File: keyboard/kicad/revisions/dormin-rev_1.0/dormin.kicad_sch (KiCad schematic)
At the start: 109 parts, among them J2 Conn_01x04_Pin, J3 Pogo Connector, Q1 HX2302A, SW1 SW_Push, SW10 SW_Push, SW11 SW_Push, SW12 SW_Push, SW13 SW_Push, SW14 SW_Push, SW15 SW_Push, SW16 SW_Push, SW17 SW_Push, SW18 SW_Push, SW19 SW_Push, SW2 SW_Push, SW20 SW_Push, SW3 SW_Push, SW4 SW_Push, SW5 SW_Push, SW6 SW_Push, SW7 SW_Push, SW8 SW_Push, SW9 SW_Push, U3 XIAO-nRF52840-Plus-SMD, U4 TPD2E2U06DCK

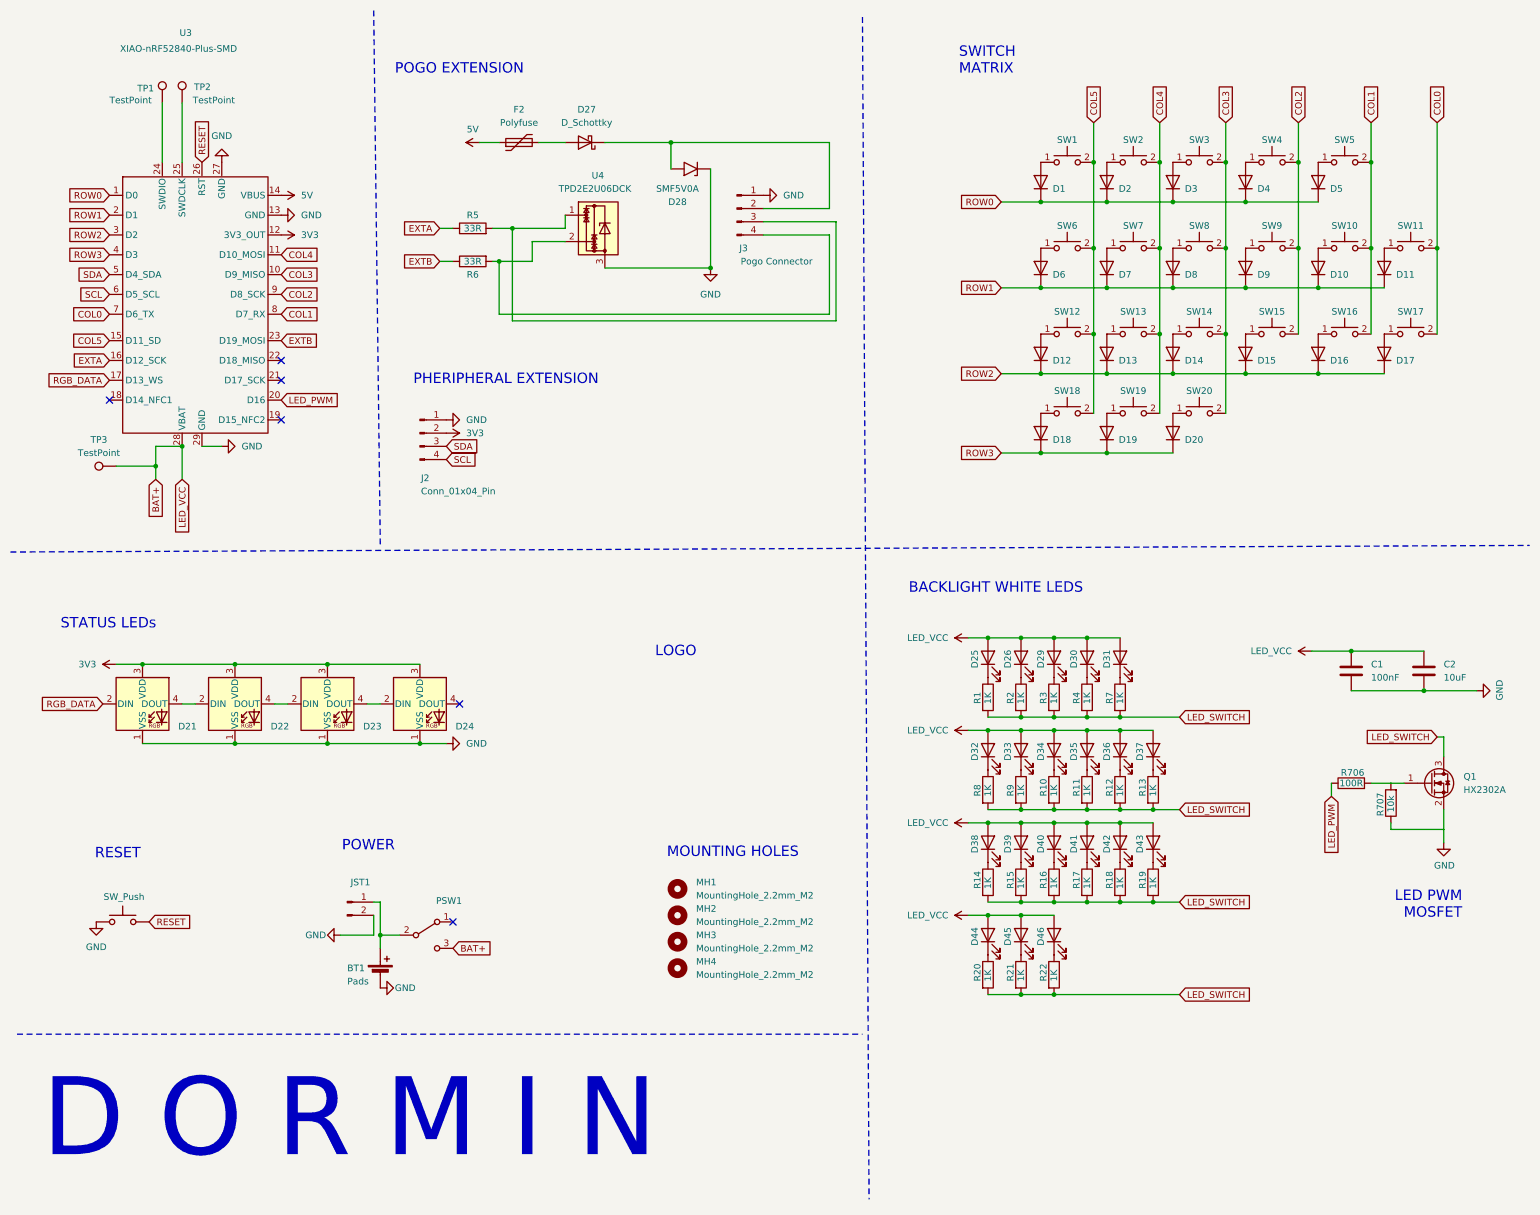
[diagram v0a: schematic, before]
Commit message: feat: added 3dmodels and improve components placement
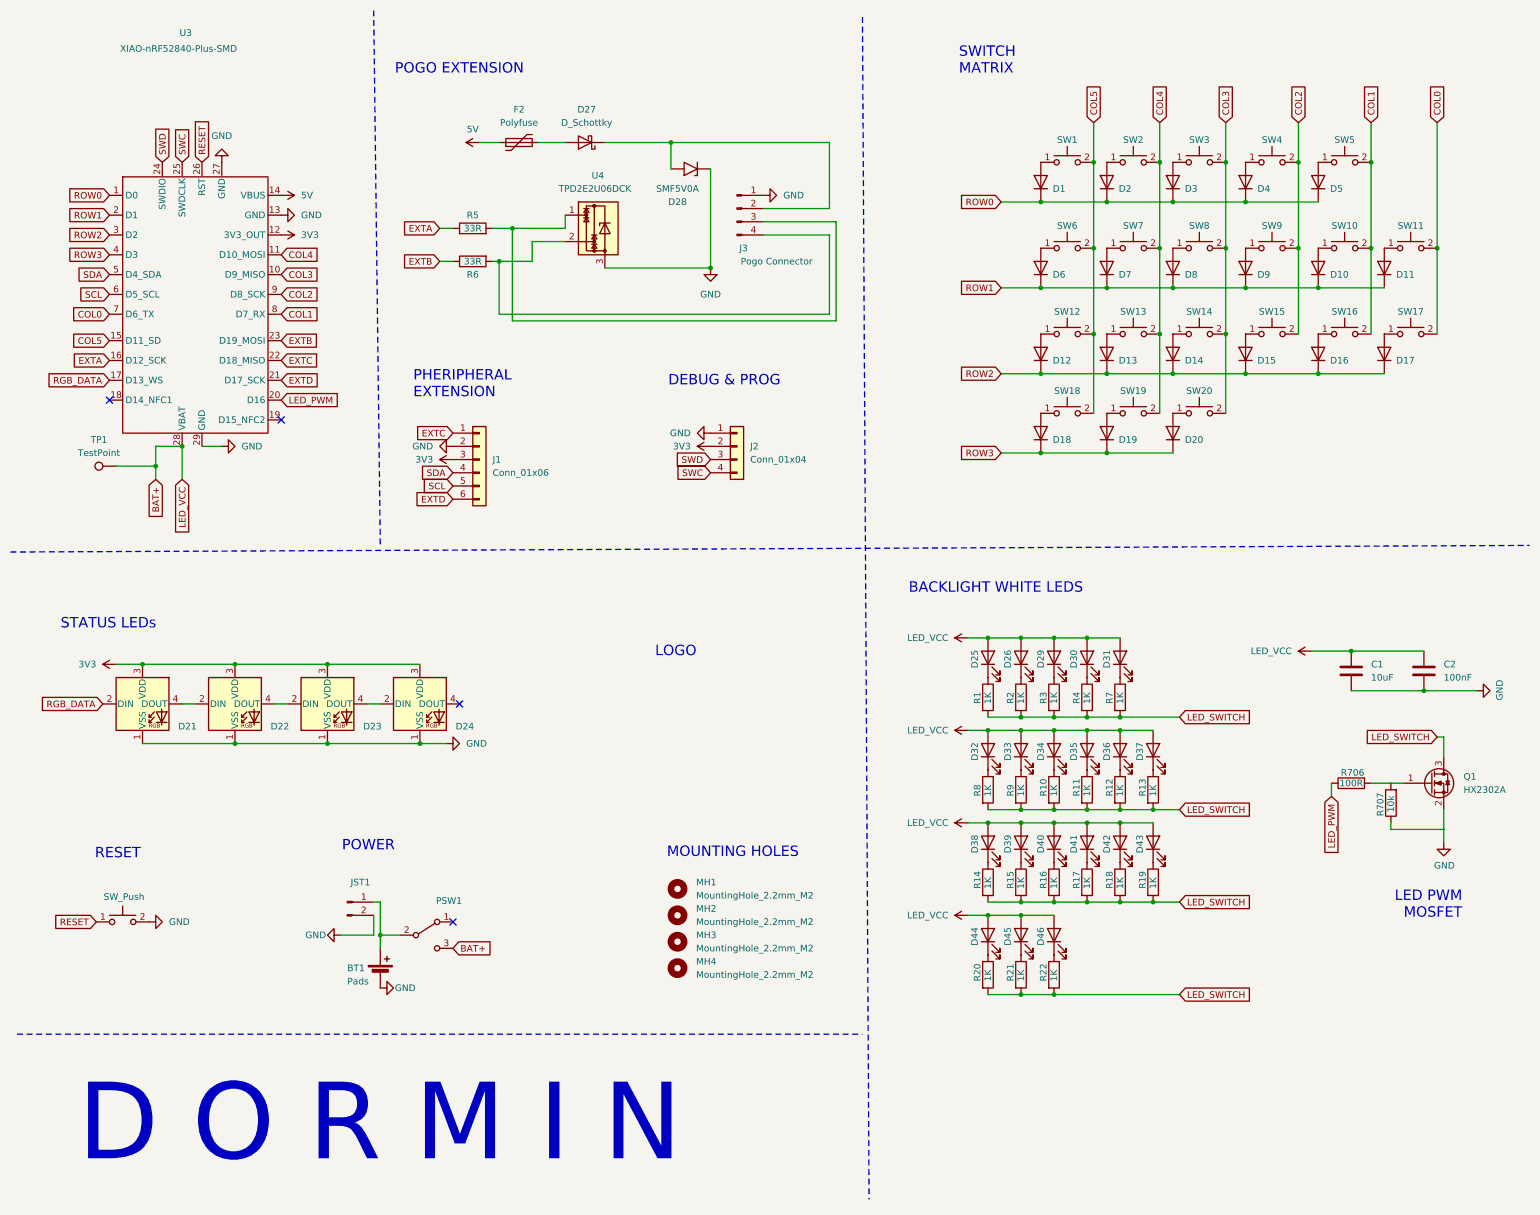
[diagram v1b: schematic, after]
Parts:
- removed J2: Conn_01x04_Pin, symbol Connector:Conn_01x04_Pin
- removed TP1, TP2: TestPoint, symbol Connector:TestPoint
- added J1: Conn_01x06, Connector_PinSocket_1.00mm:PinSocket_1x06_P1.00mm_Vertical, symbol Connector_Generic:Conn_01x06
- added J2: Conn_01x04, Connector_PinSocket_1.00mm:PinSocket_1x04_P1.00mm_Vertical, symbol Connector_Generic:Conn_01x04
- C1: value 100nF -> 10uF
- C2: value 10uF -> 100nF
- J3: footprint Connector_PinSocket_2.54mm:PinSocket_1x04_P2.54mm_Vertical_SMD_Pin1Left -> willkeebs_components:MAGNET_CONN_5x2_54mm_THT
- renumbered TP3 to TP1
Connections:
- net 3V3: now also J1.3 (Pin_3), J2.2 (Pin_2)
- net GND: now also RSW1.2, J1.2 (Pin_2), J2.1 (Pin_1); no longer RSW1.1
- net RESET: now also RSW1.1; no longer RSW1.2
- net SCL: now also J1.5 (Pin_5)
- net SDA: now also J1.4 (Pin_4)
- net SWC: now reaches U3.25 (SWDCLK)
- net SWC: now also J2.4 (Pin_4)
- net SWD: now reaches U3.24 (SWDIO)
- net SWD: now also J2.3 (Pin_3)
- net EXTD: now reaches U3.21 (D17_SCK)
- net EXTD: now also J1.6 (Pin_6)
- net EXTC: now reaches U3.22 (D18_MISO)
- net EXTC: now also J1.1 (Pin_1)
- no-connect marks 6 -> 4
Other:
- note added: "DEBUG & PROG"

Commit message: feat: updated schematics
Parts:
- removed J3: Pogo Connector, willkeebs_components:MAGNET_CONN_5x2_54mm_THT, symbol Connector:Conn_01x04_Pin
- added J4: Conn_01x04, Connector_PinSocket_2.54mm:PinSocket_1x04_P2.54mm_Vertical, symbol Connector_Generic:Conn_01x04
- J1: footprint Connector_PinSocket_1.00mm:PinSocket_1x06_P1.00mm_Vertical -> Connector_PinSocket_2.54mm:PinSocket_1x06_P2.54mm_Vertical
- J2: footprint Connector_PinSocket_1.00mm:PinSocket_1x04_P1.00mm_Vertical -> Connector_PinSocket_2.54mm:PinSocket_1x04_P2.54mm_Vertical
- RSW1: value SW_Push -> RSW1
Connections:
- net EXTC is gone; now on net EXTA: J1.1 (Pin_1), U3.22 (D18_MISO)
- net EXTD is gone; now on net EXTB: J1.6 (Pin_6), U3.21 (D17_SCK)
- net COL0: now also U3.15 (D11_SD); no longer U3.7 (D6_TX)
- net COL1: now also U3.16 (D12_SCK); no longer U3.8 (D7_RX)
- net COL5: now also U3.23 (D19_MOSI); no longer U3.15 (D11_SD)
- net EXTA: no longer R5.1, U3.16 (D12_SCK)
- net EXTB: no longer R6.1, U3.23 (D19_MOSI)
- net GND: now also J4.1 (Pin_1)
- net at R5.2, U4.1: now also J4.3 (Pin_3)
- net at D27.1 (K), D28.2 (A2): now also J4.2 (Pin_2)
- net at R6.2, U4.2: now also J4.4 (Pin_4)
- net VBAT_RAW: now reaches BT1.1 (+), JST1.1 (Pin_1), PSW1.2 (B)
- net LED_VCC renamed VBAT
- new net RX: R6.1, U3.8 (D7_RX)
- new net TX: R5.1, U3.7 (D6_TX)
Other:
- moved on the sheet: BT1, D27, D28, F2, JST1, PSW1, R5, R6, TP1, U4

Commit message: feat: organize pcb components placements
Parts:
- removed J4: Conn_01x04, Connector_PinSocket_2.54mm:PinSocket_1x04_P2.54mm_Vertical, symbol Connector_Generic:Conn_01x04
- added J3: Conn_01x05, willkeebs_misc:SMD_Conn_1x04_P2.54mm_Vertical, symbol Connector_Generic:Conn_01x05
- added R23: 100R, Resistor_SMD:R_0402_1005Metric, symbol Device:R
- J1: footprint Connector_PinSocket_2.54mm:PinSocket_1x06_P2.54mm_Vertical -> willkeebs_misc:SMD_Conn_1x06_P2.54mm_Vertical
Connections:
- net EXTA: now also U3.21 (D17_SCK); no longer U3.22 (D18_MISO)
- net EXTB: now also U3.22 (D18_MISO); no longer U3.21 (D17_SCK)
- net GND: now also J3.1 (Pin_1)
- net SCL: now also J1.4 (Pin_4); no longer J1.5 (Pin_5)
- net SDA: now also J1.5 (Pin_5); no longer J1.4 (Pin_4)
- net SWC: now also J2.3 (Pin_3); no longer J2.4 (Pin_4)
- net SWD: now also J2.4 (Pin_4); no longer J2.3 (Pin_3)
- net at R5.2, U4.1: now also J3.4 (Pin_4)
- net at D27.1 (K), D28.2 (A2): now also J3.2 (Pin_2)
- net at R6.2, U4.2: now also J3.3 (Pin_3)
- net DETECT: now reaches U3.18 (D14_NFC1)
- net DETECT: now also R23.1
- new net: J3.5 (Pin_5), R23.2
- no-connect marks 4 -> 3
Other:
- note added: "DEBUG"
- note added: "EXTENTIONS"
- note added: "PHERIPHERAL"
- note added: "POGO Connector"
- note removed: "DEBUG & PROG"
- note removed: "PHERIPHERAL EXTENSION"
- note removed: "POGO EXTENSION"
- moved on the sheet: D27, D28, F2, J1, R5, R6, U4

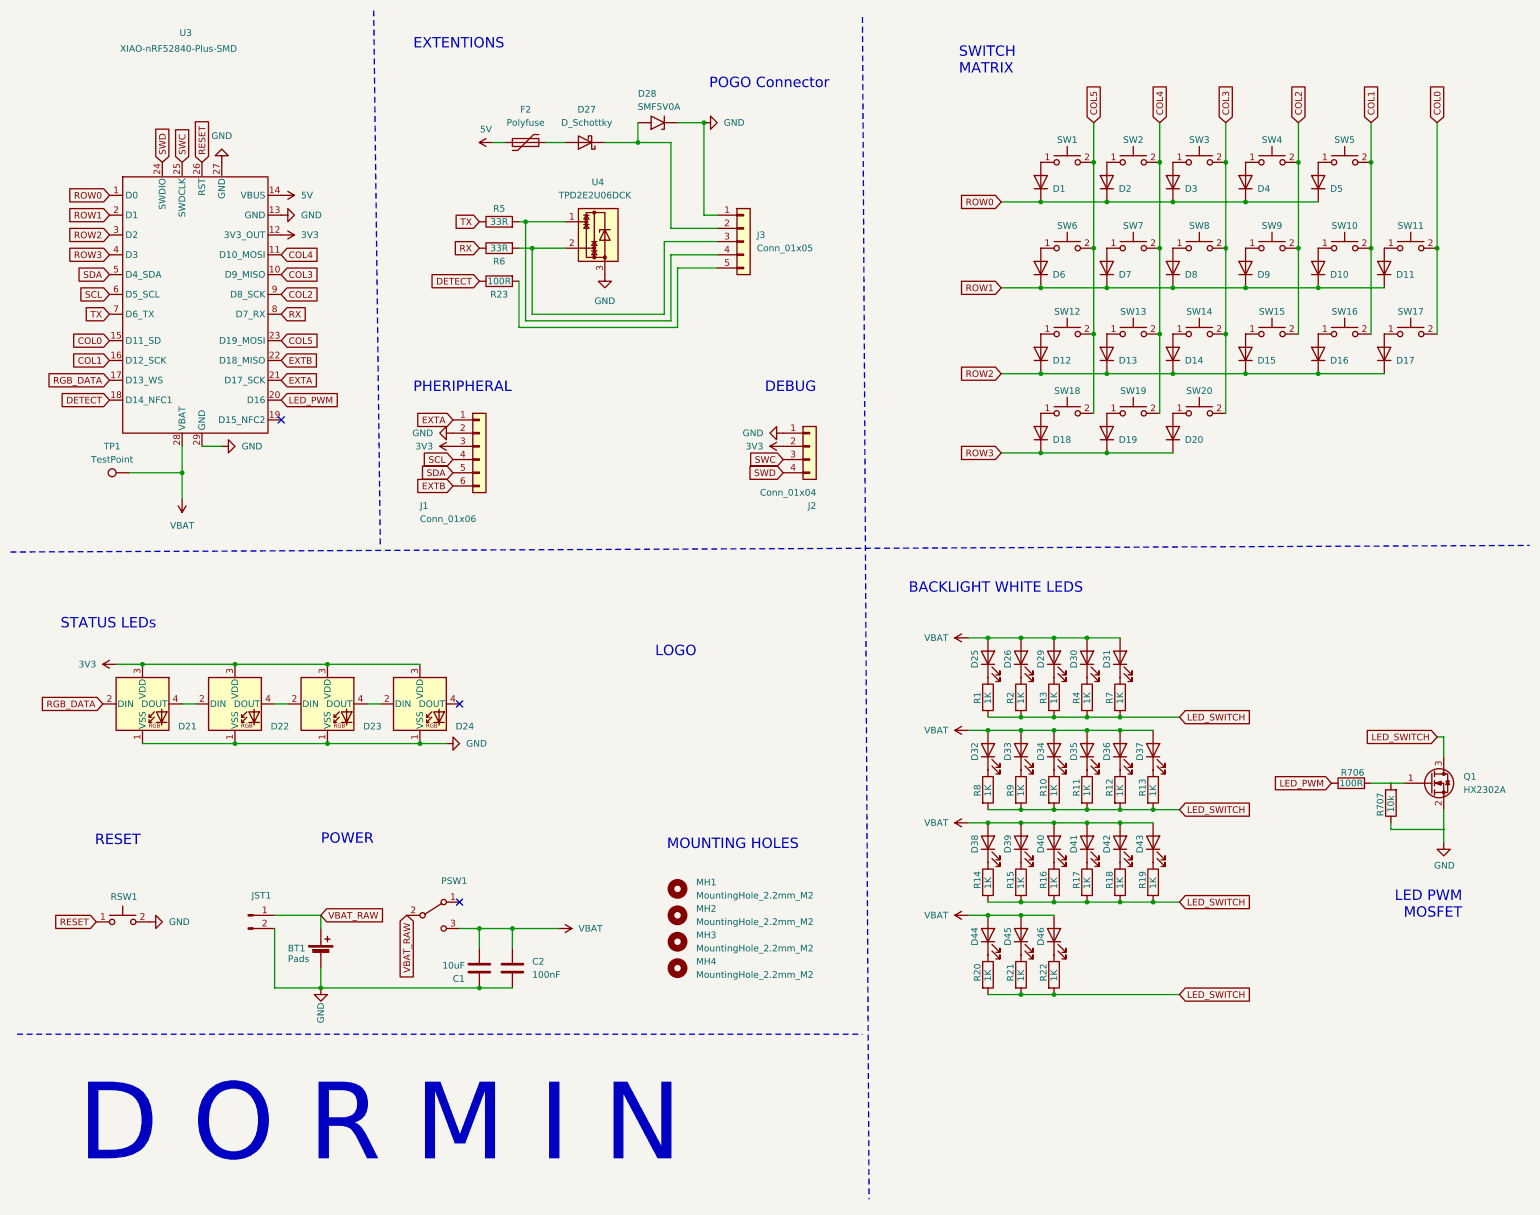
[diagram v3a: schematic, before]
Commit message: feat: implemented better status-led-system
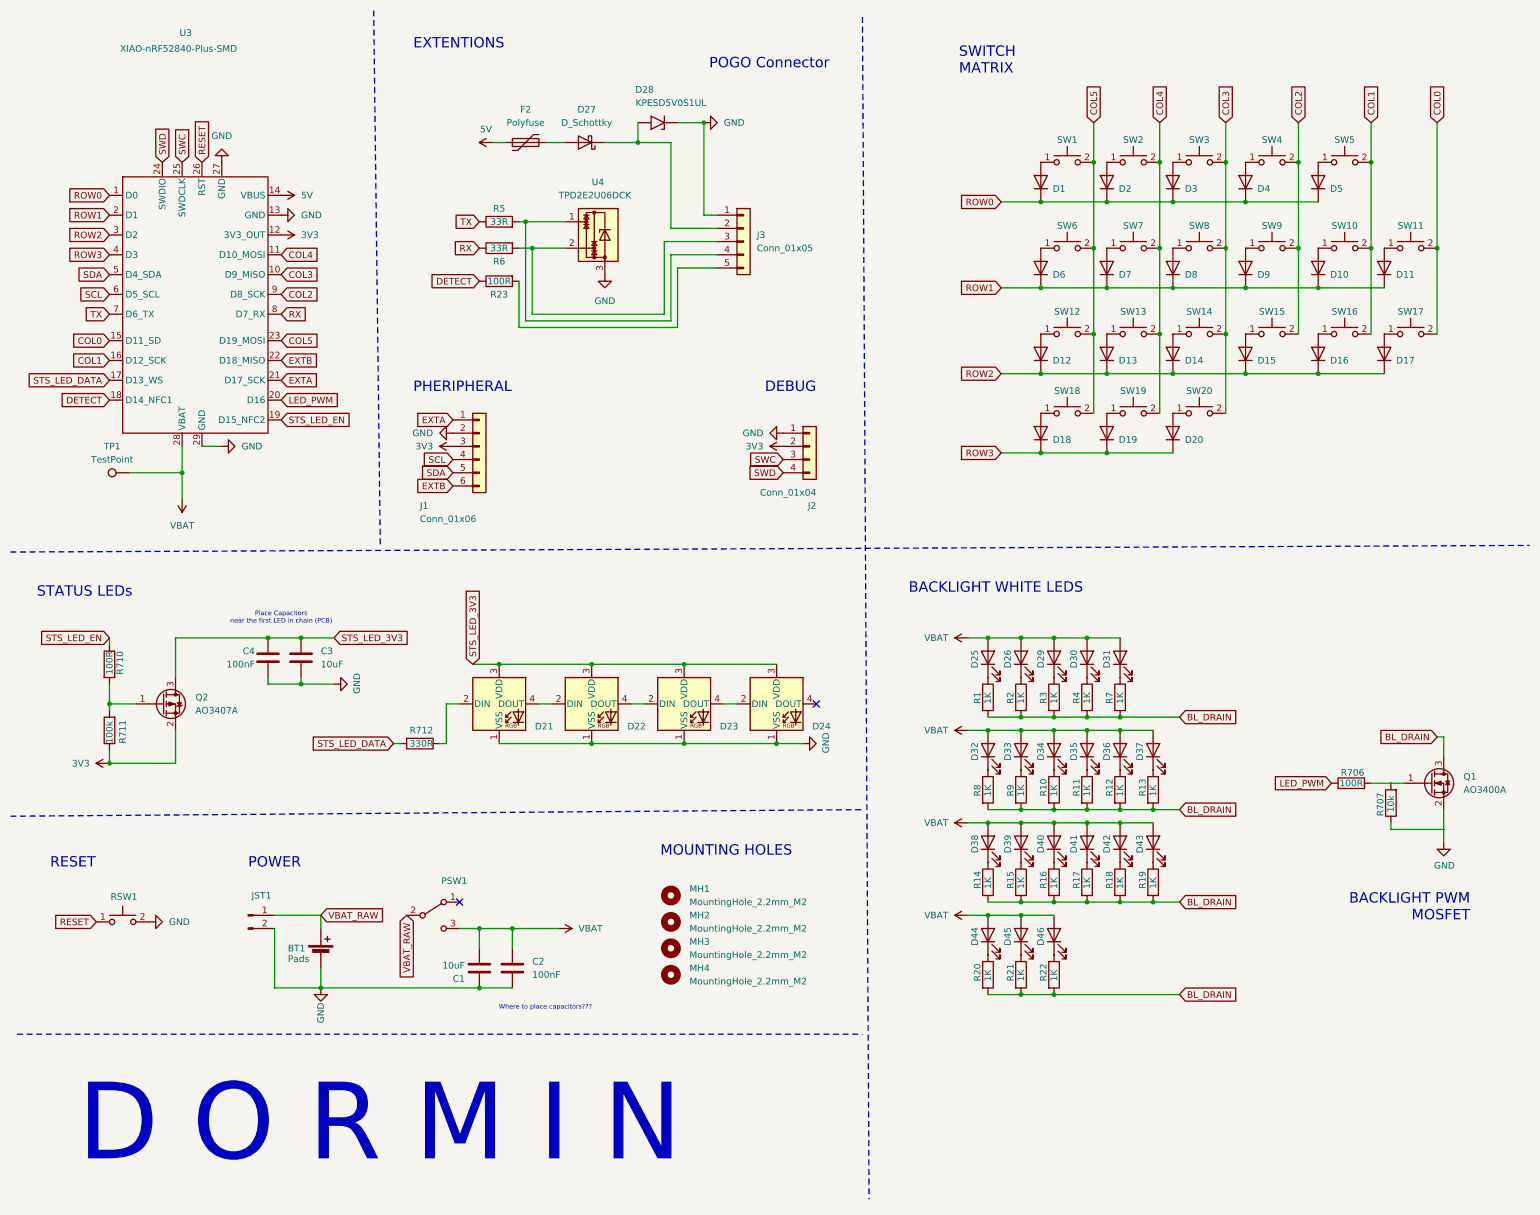
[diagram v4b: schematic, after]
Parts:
- added C3: 10uF, Capacitor_SMD:C_0603_1608Metric, symbol Device:C
- added C4: 100nF, Capacitor_SMD:C_0603_1608Metric, symbol Device:C
- added Q2: AO3407A, Package_TO_SOT_SMD:SOT-23, symbol Transistor_FET:AO3401A
- added R710: 100R, Resistor_SMD:R_0603_1608Metric, symbol Device:R
- added R711: 100k, Resistor_SMD:R_0603_1608Metric, symbol Device:R
- added R712: 330R, Resistor_SMD:R_0603_1608Metric, symbol Device:R
- C1, C2: MFPN (none) -> CL10A106KP8NNNC
- D27: footprint Diode_SMD:Nexperia_CFP3_SOD-123W -> Diode_SMD:D_SOD-523; MFPN (none) -> BAT54C
- D28: value SMF5V0A -> KPESD5V0S1UL; footprint Diode_SMD:D_SMF -> Diode_SMD:D_SOD-882; MFPN (none) -> KPESD5V0S1UL
- Q1: value HX2302A -> AO3400A; MFP HX2302A -> (none); MFPN (none) -> AO3400A
- R23: footprint Resistor_SMD:R_0402_1005Metric -> Resistor_SMD:R_0603_1608Metric; MFPN (none) -> 0603WAF1000T5E
- R5, R6: footprint Resistor_SMD:R_0402_1005Metric -> Resistor_SMD:R_0603_1608Metric; MFPN (none) -> 0603WAF330JT5E
- U4: MFPN (none) -> TPD2E2U06DCK
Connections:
- net 3V3: now also Q2.2 (S), R711.1; no longer D21.3 (VDD), D22.3 (VDD), D23.3 (VDD), D24.3 (VDD)
- net GND: now also C3.1, C4.2
- net STS_LED_EN: now reaches U3.19 (D15_NFC2)
- net STS_LED_EN: now also R710.1
- net LED_SWITCH renamed BL_DRAIN
- net RGB_DATA: no longer names the net of D21.2 (DIN)
- net RGB_DATA: now also R712.1; no longer U3.17 (D13_WS)
- new net: Q2.1 (G), R710.2, R711.2
- new net STS_LED_3V3: C3.2, C4.1, D21.3 (VDD), D22.3 (VDD), D23.3 (VDD), D24.3 (VDD), Q2.3 (D)
- new net STS_LED_DATA: R712.2, U3.17 (D13_WS)
- no-connect marks 3 -> 2
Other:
- note added: "BACKLIGHT PWM MOSFET"
- note added: "Place Capacitors near the first LED in chain (PCB)"
- note added: "Where to place capacitors???"
- note removed: "LED PWM MOSFET"
- note removed: "LOGO"
- moved on the sheet: D21, D22, D23, D24, MH1, MH2, MH3, MH4
